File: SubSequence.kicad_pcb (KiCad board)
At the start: 2 copper layers, 80.3 x 100 mm, 52 parts, among them J1 Conn_02x03_Odd_Even, J2 Conn_02x03_Odd_Even, J3 Conn_01x03, SW1 SW_Push, SW2 SW_SPDT_MSM, SW3 SW_SPDT_MSM, SW4 SW_SPDT_MSM, SW5 SW_SPDT_MSM, SW6 SW_SPDT_MSM, SW7 SW_SPDT_MSM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

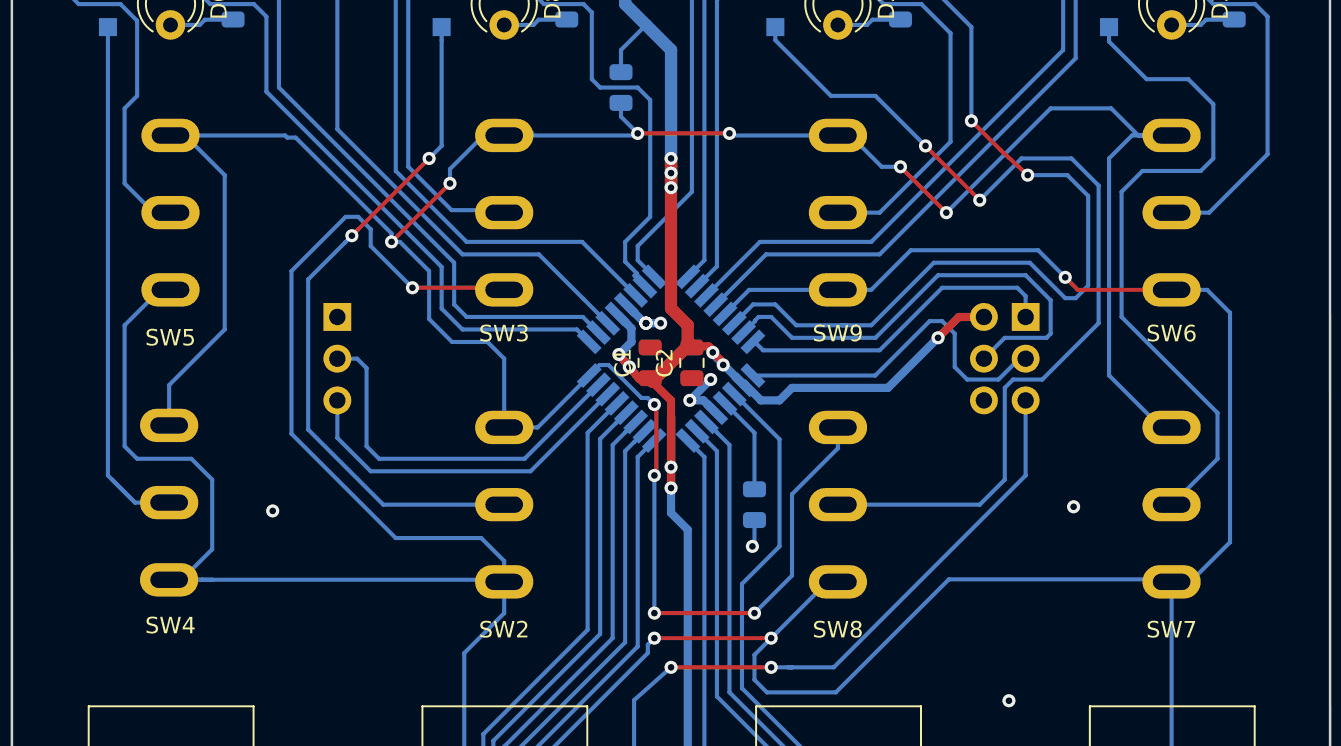
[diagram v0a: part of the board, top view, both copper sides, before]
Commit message: Initial revision B of board, now using PCB mounted SPDT.
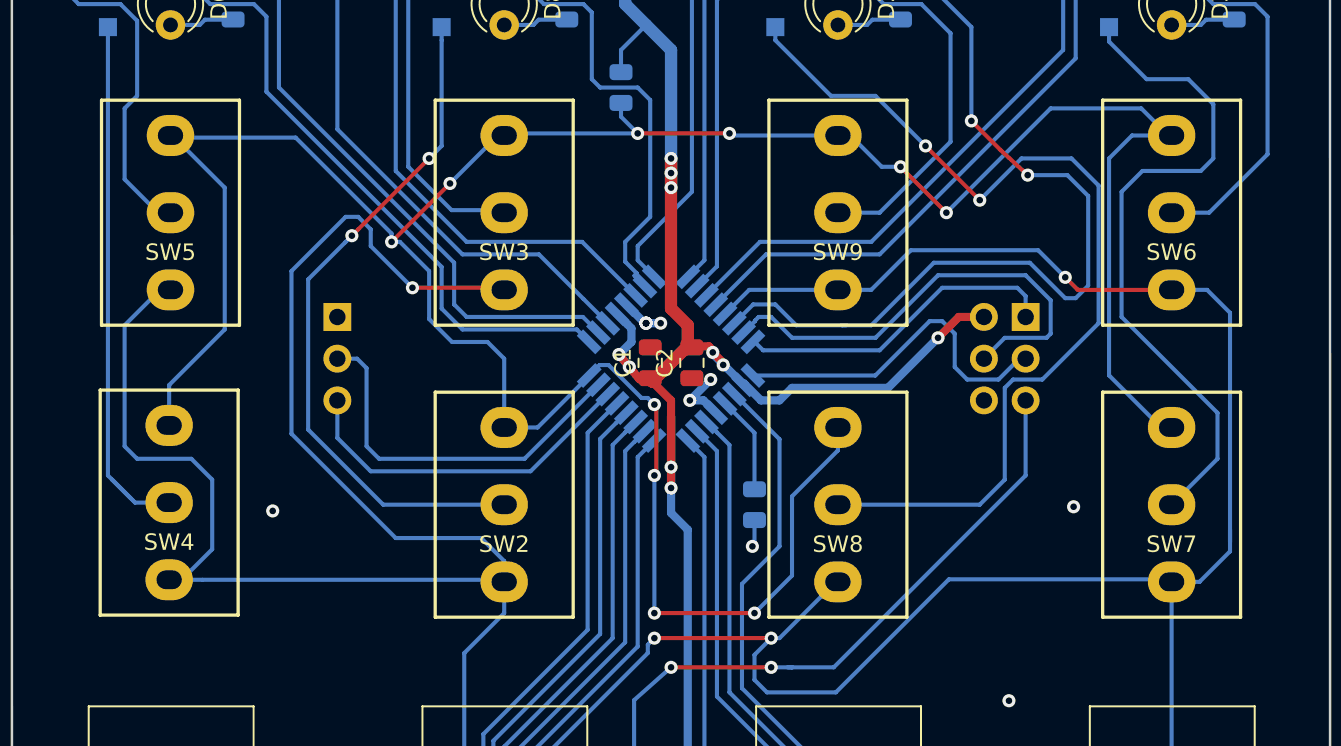
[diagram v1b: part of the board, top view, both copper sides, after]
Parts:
- SW2, SW3, SW4, SW5, SW6, SW7, SW8, SW9: footprint Local:SP1MS1 -> Local:SPDT
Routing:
- net /MCU328/PD2: track 180.8 -> 178.1 mm
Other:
- board text added: "Marangisto 2018"
- board text added: "Rev B"
- board text removed: "Rev A"
- board text removed: "© Marangisto 2018"
